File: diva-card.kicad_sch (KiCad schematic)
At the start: 0 parts

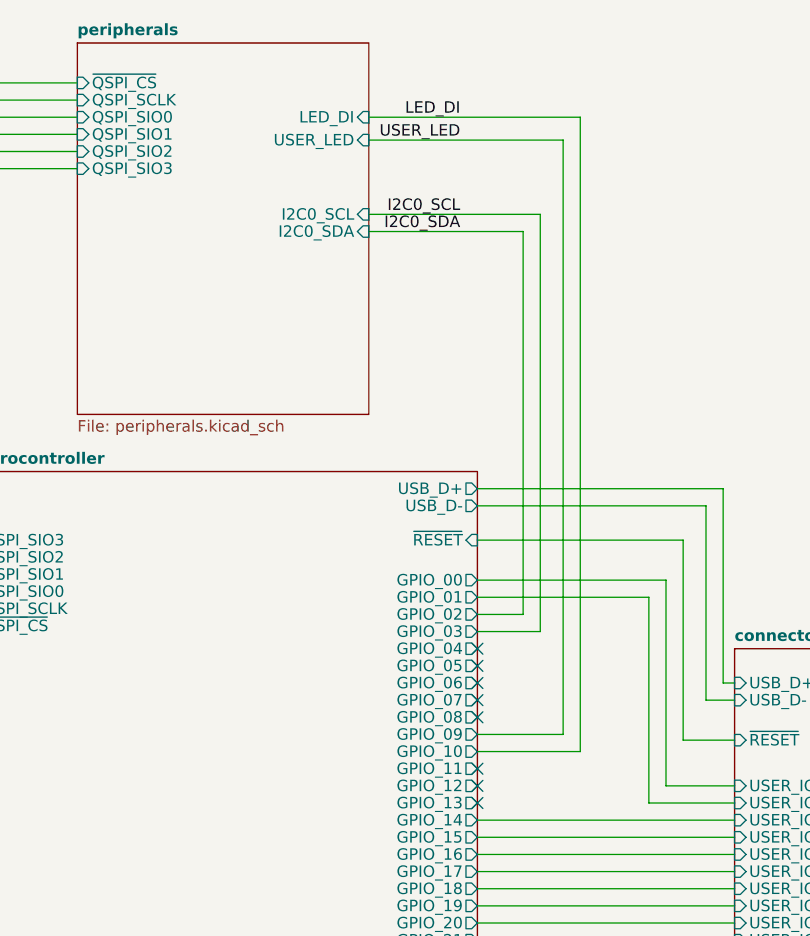
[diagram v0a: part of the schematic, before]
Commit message: Basic routing complete, rename
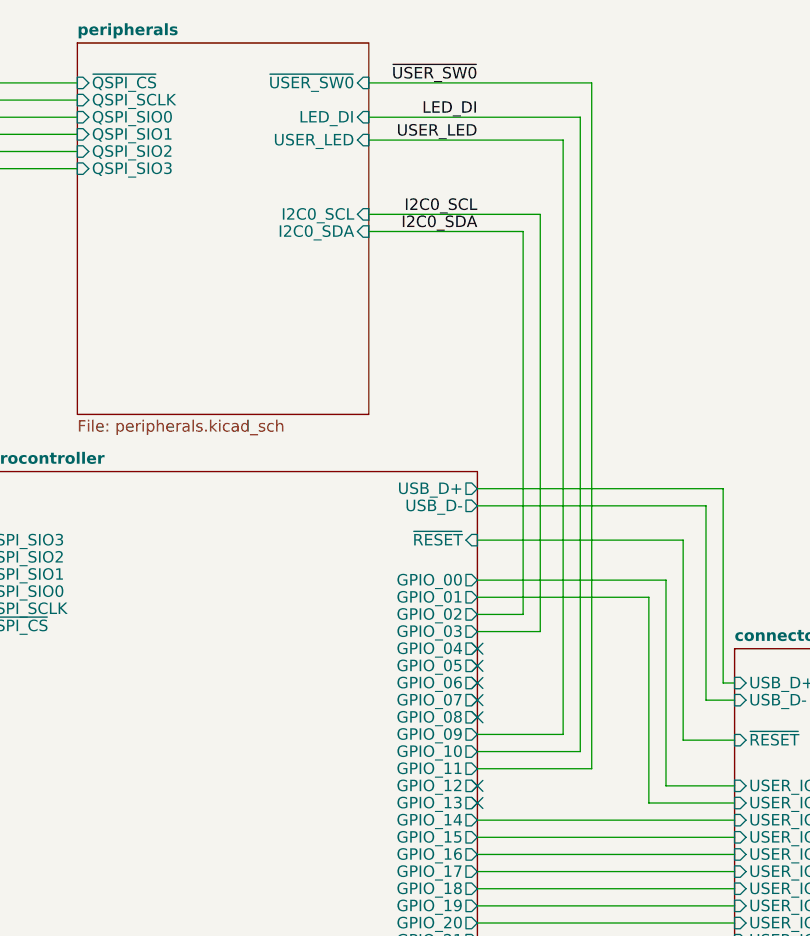
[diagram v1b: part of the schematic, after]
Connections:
- no-connect marks 13 -> 12
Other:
- sheet peripherals ports: added ~{USER_SW0}; removed none

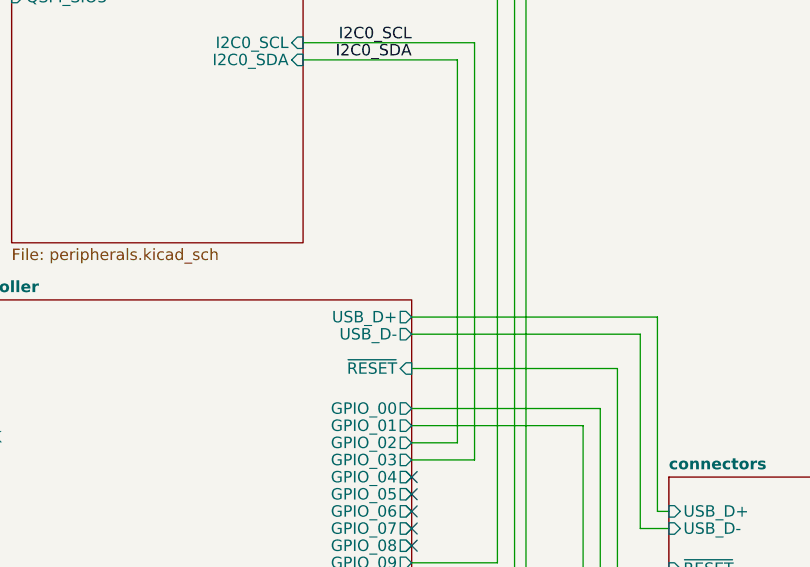
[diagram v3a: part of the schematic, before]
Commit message: Adding schematic pdf
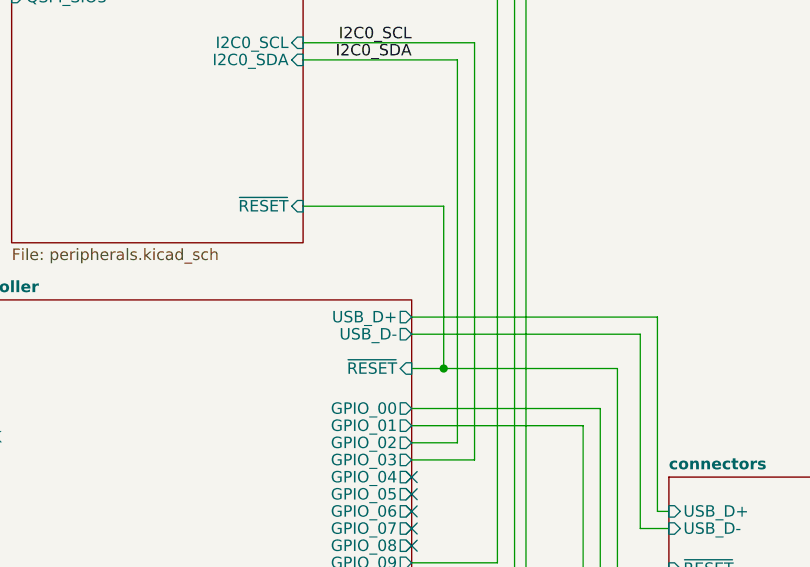
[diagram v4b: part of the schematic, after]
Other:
- sheet peripherals ports: added ~{RESET}; removed none
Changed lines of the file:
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@@
     (company "DIVA ENG")
+  )
+  (junction (at 169.291 76.835) (diameter 0) (color 0 0 0 0)
   )
   (no_connect (at 165.735 104.14))
@@
     (stroke (width 0) (type default) (color 0 0 0 0))
   )
+  (wire (pts (xy 169.291 58.801) (xy 169.291 76.835))
+    (stroke (width 0) (type default) (color 0 0 0 0))
+  )
   (wire (pts (xy 165.735 145.415) (xy 190.5 145.415))
     (stroke (width 0) (type default) (color 0 0 0 0))
@@
     (stroke (width 0) (type default) (color 0 0 0 0))
   )
+  (wire (pts (xy 153.67 58.801) (xy 169.291 58.801))
+    (stroke (width 0) (type default) (color 0 0 0 0))
+  )
   (wire (pts (xy 188.595 99.06) (xy 194.31 99.06))
     (stroke (width 0) (type default) (color 0 0 0 0))
@@
     (stroke (width 0) (type default) (color 0 0 0 0))
   )
-  (wire (pts (xy 165.735 76.835) (xy 188.595 76.835))
+  (wire (pts (xy 165.735 76.835) (xy 169.291 76.835))
     (stroke (width 0) (type default) (color 0 0 0 0))
   )
@@
   )
   (wire (pts (xy 109.22 84.455) (xy 85.09 84.455))
+    (stroke (width 0) (type default) (color 0 0 0 0))
+  )
+  (wire (pts (xy 169.291 76.835) (xy 188.595 76.835))
     (stroke (width 0) (type default) (color 0 0 0 0))
   )
@@
     )
     (pin "~{USER_SW0}" input (at 153.67 26.035 0)
+      (effects (font (size 1.27 1.27)) (justify right))
+    )
+    (pin "~{RESET}" input (at 153.67 58.801 0)
       (effects (font (size 1.27 1.27)) (justify right))
     )
@@
       (reference "#PWR078") (unit 1) (value "VBUS") (footprint "")
     )
+    (path "/edc51190-cad1-4c5e-beb6-0b752ab7f2ca/9d03955f-1947-4624-ada8-0f32d6d02be5"
+      (reference "#PWR079") (unit 1) (value "GND") (footprint "")
+    )
     (path "/c6be3312-b21a-44a1-9087-4385ef7236e6/f637fcd5-98e3-40f6-8691-ff60029952aa"
       (reference "#PWR083") (unit 1) (value "GND") (footprint "")
@@
       (reference "#PWR0107") (unit 1) (value "+5V") (footprint "")
     )
-    (path "/c6be3312-b21a-44a1-9087-4385ef7236e6/4164492f-2c57-4d1f-a3be-9f4d3d5b78fe"
-      (reference "#PWR?") (unit 1) (value "GND") (footprint "")
-    )
-    (path "/c6be3312-b21a-44a1-9087-4385ef7236e6/a1928a95-ff0b-42bc-9da3-5b5aea83bedf"
-      (reference "#PWR?") (unit 1) (value "+3.3V") (footprint "")
-    )
     (path "/6ea7b2ea-28e4-4ca5-9b05-9fcac11f3492/05f879d7-042f-43bd-bcde-728faaa5380d"
       (reference "C1") (unit 1) (value "10u") (footprint "Capacitor_SMD:C_0603_1608Metric")
@@
     )
     (path "/ef153473-0ff6-41c4-b5ea-5e2451c67924/e789dd01-de87-4745-a5fb-cd97ab006622"
-      (reference "C21") (unit 1) (value "22p") (footprint "Capacitor_SMD:C_0402_1005Metric")
+      (reference "C21") (unit 1) (value "33p") (footprint "Capacitor_SMD:C_0402_1005Metric")
     )
     (path "/ef153473-0ff6-41c4-b5ea-5e2451c67924/eea742b7-fa0a-4e0d-bd51-357e9e98f7ec"
-      (reference "C22") (unit 1) (value "22p") (footprint "Capacitor_SMD:C_0402_1005Metric")
+      (reference "C22") (unit 1) (value "33p") (footprint "Capacitor_SMD:C_0402_1005Metric")
     )
     (path "/edc51190-cad1-4c5e-beb6-0b752ab7f2ca/ca13edc2-6634-4c38-af2a-c13c8e0045a7"
@@
       (reference "D2") (unit 1) (value "WHITE") (footprint "LED_SMD:LED_0402_1005Metric")
     )
+    (path "/edc51190-cad1-4c5e-beb6-0b752ab7f2ca/b560523c-206a-4f3e-b1ea-fd5801d1bde0"
+      (reference "FID1") (unit 1) (value "Fiducial") (footprint "Fiducial:Fiducial_0.5mm_Mask1mm")
+    )
+    (path "/edc51190-cad1-4c5e-beb6-0b752ab7f2ca/86bc5b15-f8e0-48b3-be85-a50a40e50539"
+      (reference "FID2") (unit 1) (value "Fiducial") (footprint "Fiducial:Fiducial_0.5mm_Mask1mm")
+    )
     (path "/c6be3312-b21a-44a1-9087-4385ef7236e6/87c1979f-1077-48a2-b4c6-b21b214c3569"
       (reference "J1") (unit 1) (value "Conn_02x05_Odd_Even") (footprint "Connector:Tag-Connect_TC2050-IDC-NL_2x05_P1.27mm_Vertical")
@@
       (reference "J3") (unit 1) (value "Conn_02x21_Odd_Even") (footprint "Diva-Card:PICO_CARD_EDGE_21")
     )
-    (path "/c6be3312-b21a-44a1-9087-4385ef7236e6/e44f783f-40cd-47c5-92be-9be34ec24857"
-      (reference "J?") (unit 1) (value "Conn_02x05_Odd_Even") (footprint "Connector:Tag-Connect_TC2050-IDC-NL_2x05_P1.27mm_Vertical")
-    )
     (path "/edc51190-cad1-4c5e-beb6-0b752ab7f2ca/8d75b3e4-384b-4424-ba24-5872431aceb1"
       (reference "L1") (unit 1) (value "WS2812C") (footprint "Diva-Card:WS2812C-2020")
@@
     )
     (path "/edc51190-cad1-4c5e-beb6-0b752ab7f2ca/9e524dfe-0435-4f91-b4f5-4736c1613521"
-      (reference "R5") (unit 1) (value "10k") (footprint "Resistor_SMD:R_0402_1005Metric")
+      (reference "R5") (unit 1) (value "1k") (footprint "Resistor_SMD:R_0402_1005Metric")
     )
     (path "/edc51190-cad1-4c5e-beb6-0b752ab7f2ca/01e4fd07-5b31-43d0-a2bd-20174657f8a0"
@@
     )
     (path "/edc51190-cad1-4c5e-beb6-0b752ab7f2ca/d2aee038-377d-409f-acc7-eec4c7ef9061"
-      (reference "SW1") (unit 1) (value "SW_Push") (footprint "Diva-Card:SW_TS-1187A-B-A-B")
+      (reference "SW1") (unit 1) (value "USER") (footprint "Diva-Card:SW_TS-1187A-B-A-B")
     )
     (path "/edc51190-cad1-4c5e-beb6-0b752ab7f2ca/4a74d3aa-cefe-4342-b173-9857f8da9dbe"
-      (reference "SW2") (unit 1) (value "SW_Push") (footprint "Diva-Card:SW_TS-1187A-B-A-B")
+      (reference "SW2") (unit 1) (value "BOOTSEL") (footprint "Diva-Card:SW_TS-1187A-B-A-B")
+    )
+    (path "/edc51190-cad1-4c5e-beb6-0b752ab7f2ca/f944bc9a-206e-4da3-bfc1-49e0e9d675ef"
+      (reference "SW3") (unit 1) (value "RESET") (footprint "Diva-Card:SW_TS-1187A-B-A-B")
     )
     (path "/6ea7b2ea-28e4-4ca5-9b05-9fcac11f3492/372ac643-95c8-474d-a22d-d937aebd3d35"
@@
     )
     (path "/ef153473-0ff6-41c4-b5ea-5e2451c67924/a31ab699-1c83-4eac-a2d4-8ac2fa73e7bf"
-      (reference "Y1") (unit 1) (value "Crystal_GND24") (footprint "Crystal:Crystal_SMD_3225-4Pin_3.2x2.5mm")
-    )
-  )
+      (reference "Y1") (unit 1) (value "X322512MSB4SI") (footprint "Crystal:Crystal_SMD_3225-4Pin_3.2x2.5mm")
+    )
+  )
